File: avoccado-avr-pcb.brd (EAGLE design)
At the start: 17.8 x 41 mm, 30 parts, among them IC1 MCP1703CB, IC5 ATMEGA328P-20MU, Q1 16MHz, Q2 MOSFET-NCHANNEL2N7002PW, U1 ATMEGA328P, U2 MCP73831, X1 Micro USB

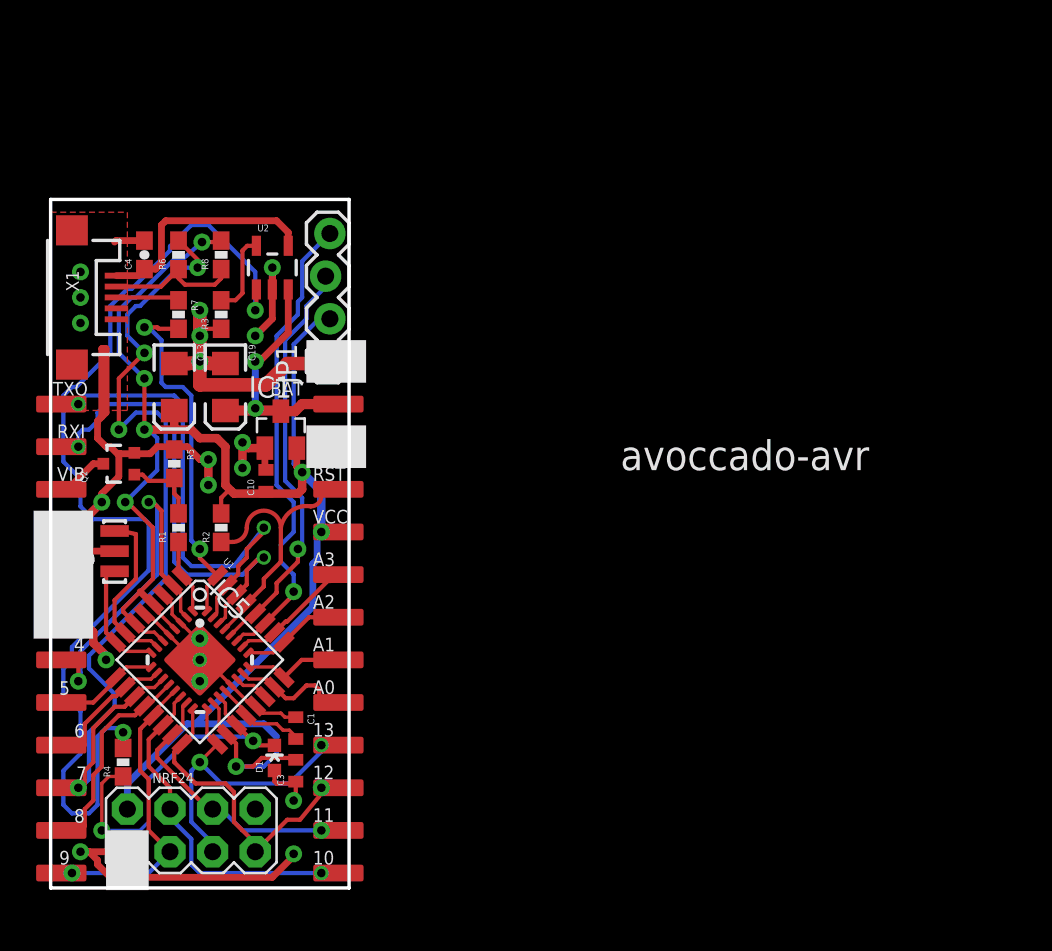
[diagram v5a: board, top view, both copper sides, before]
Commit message: change MPU6050 locked header to straight one
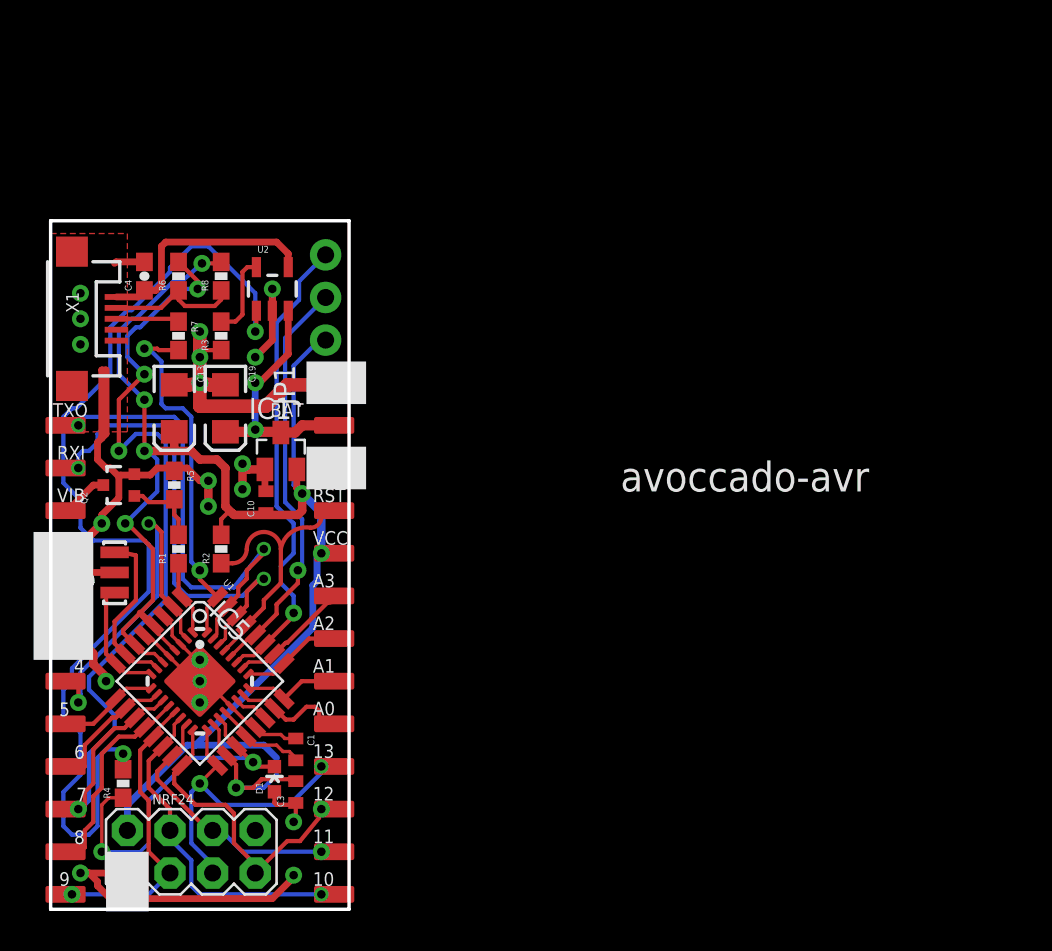
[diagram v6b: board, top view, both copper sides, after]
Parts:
- JP1: device SparkFun-Connectors:1X04_LOCK -> SparkFun-Connectors:1X04_NO_SILK
- moved JP1 1.28 mm to (16.4, 31.4)
- moved JP11 1.27 mm to (0.64, 25.0)
- moved JP3 1.27 mm to (17.1, 25.0)
- moved R3 1.27 mm to (10.2, 34.2)
- moved R7 1.27 mm to (7.62, 34.2)
- moved JP10 1.27 mm to (0.64, 14.9)
- moved JP5 1.27 mm to (17.1, 14.9)
- moved C3 1.27 mm to (14.6, 6.99)
- moved JP8 1.27 mm to (17.1, 4.70)
- moved JP9 1.27 mm to (0.64, 4.70)
- moved NRF24 1.27 mm to (8.38, 3.43)
- moved C1 1.27 mm to (14.6, 9.53)
- moved C10 1.27 mm to (12.8, 24.3)
- moved C13 1.27 mm to (7.37, 29.8)
- moved C19 1.27 mm to (10.4, 29.8)
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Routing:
- net VBAT: track 18.2 -> 17.6 mm

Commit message: silkscreen placed
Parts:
- removed IC1: MCP1703CB, linear:SOT23
- removed JP1: (no value), SparkFun-Connectors:1X04_NO_SILK
- removed U1: ATMEGA328P, SparkFun-DigitalIC:TQFP32-08
- added AVR: ATMEGA328P, SparkFun-DigitalIC:TQFP32-08
- added LDO: MCP1703CB, linear:SOT23
- added MPU6050: (no value), SparkFun-Connectors:1X04_NO_SILK
- D1: value CHARGE LED -> LED
- Q2: value MOSFET-NCHANNEL2N7002PW -> FET
- moved R7 1.15 mm to (8.23, 35.1)
- moved R3 1.15 mm to (10.8, 35.1)
- moved C13 1.15 mm to (7.98, 30.8)
- moved JP11 1.15 mm to (1.25, 26.0)
- moved Q1 1.15 mm to (4.42, 21.0)
- moved C19 1.15 mm to (11.0, 30.8)
- moved JP3 1.15 mm to (17.8, 26.0)
- moved NRF24 1.15 mm to (8.99, 4.41)
- moved D1 1.15 mm to (13.9, 8.73)
- moved JP9 1.15 mm to (1.25, 5.68)
- moved C3 1.15 mm to (15.2, 7.96)
- moved JP8 1.15 mm to (17.8, 5.68)
- moved C4 1.15 mm to (6.20, 38.7)
- moved Q2 1.15 mm to (4.67, 26.3)
- moved R1 1.15 mm to (8.23, 22.4)
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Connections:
- net 3V3: now also AVR.18, AVR.4, AVR.6, LDO.2, MPU6050.2; no longer IC1.2, JP1.2, U1.18, U1.4, U1.6
- net A0: now also AVR.23; no longer U1.23
- net A1: now also AVR.24; no longer U1.24
- net A2: now also AVR.25; no longer U1.25
- net A3: now also AVR.26; no longer U1.26
- net A4: now also AVR.27, MPU6050.4; no longer JP1.4, U1.27
- net A5: now also AVR.28, MPU6050.3; no longer JP1.3, U1.28
- net A6: now also AVR.19; no longer U1.19
- net A7: now also AVR.22; no longer U1.22
- net AREF: now also AVR.20; no longer U1.20
- net D10: now also AVR.14; no longer U1.14
- net D2: now also AVR.32; no longer U1.32
- net D3: now also AVR.1; no longer U1.1
- net D4: now also AVR.2; no longer U1.2
- net D5: now also AVR.9; no longer U1.9
- net D6: now also AVR.10; no longer U1.10
- net D7: now also AVR.11; no longer U1.11
- net D8: now also AVR.12; no longer U1.12
- net D9: now also AVR.13; no longer U1.13
- net GND: now also AVR.21, AVR.3, AVR.5, LDO.1, MPU6050.1; no longer IC1.1, JP1.1, U1.21, U1.3, U1.5
- net MISO: now also AVR.16; no longer U1.16
- net MOSI: now also AVR.15; no longer U1.15
- net N$1: now also AVR.8; no longer U1.8
- net N$2: now also AVR.7; no longer U1.7
- net RESET: now also AVR.29; no longer U1.29
- net RXI: now also AVR.30; no longer U1.30
- net SCK: now also AVR.17; no longer U1.17
- net TXO: now also AVR.31; no longer U1.31
- net VBAT: now also LDO.3; no longer IC1.3
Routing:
- net GND: track 100.8 -> 132.6 mm
- removed copper zone on layer 1, net GND
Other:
- board size 17.8 x 41 mm -> 19 x 42 mm
- board text added: "avoccado"
- board text removed: "avoccado-avr"
- board text removed: "cc-by-sa 4.0 etemu.com"
